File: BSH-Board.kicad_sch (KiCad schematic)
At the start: 10 parts, among them J1 667101210103, U1 ESP32-S2-MINI-2-N4, U3 TXS0102DQER, U5 AP63203WU

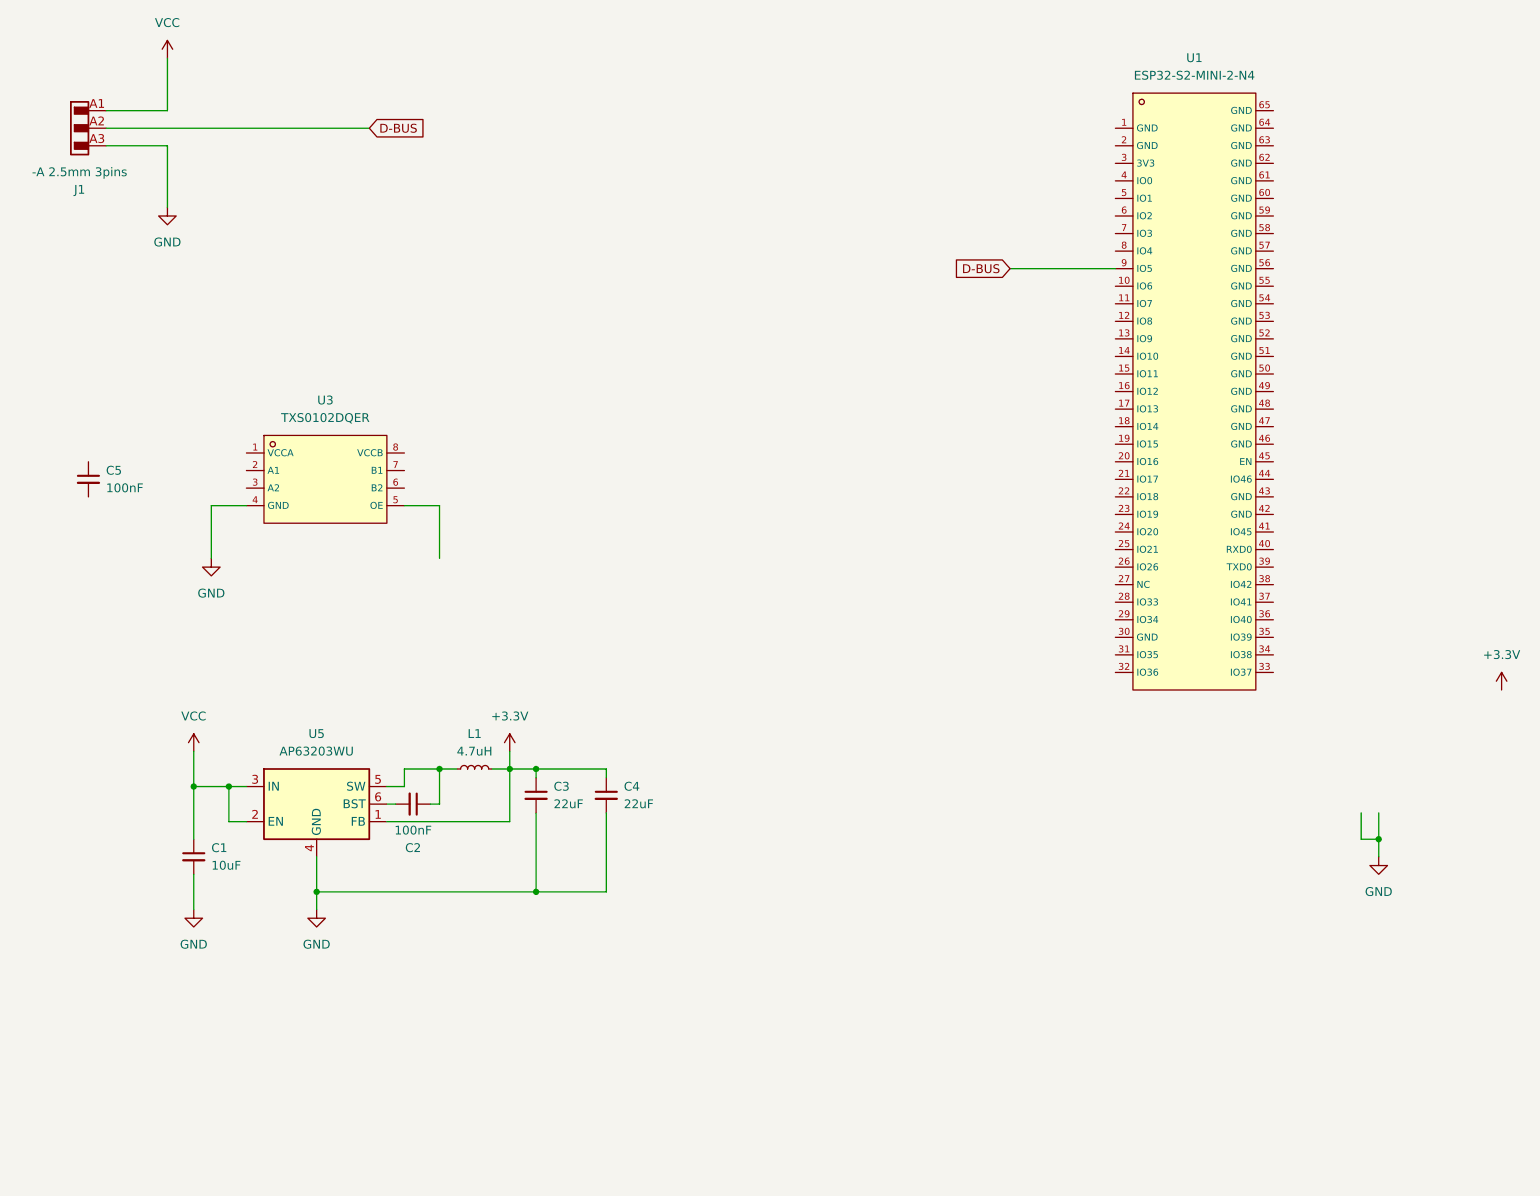
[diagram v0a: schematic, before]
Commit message: Add LDO for 5V
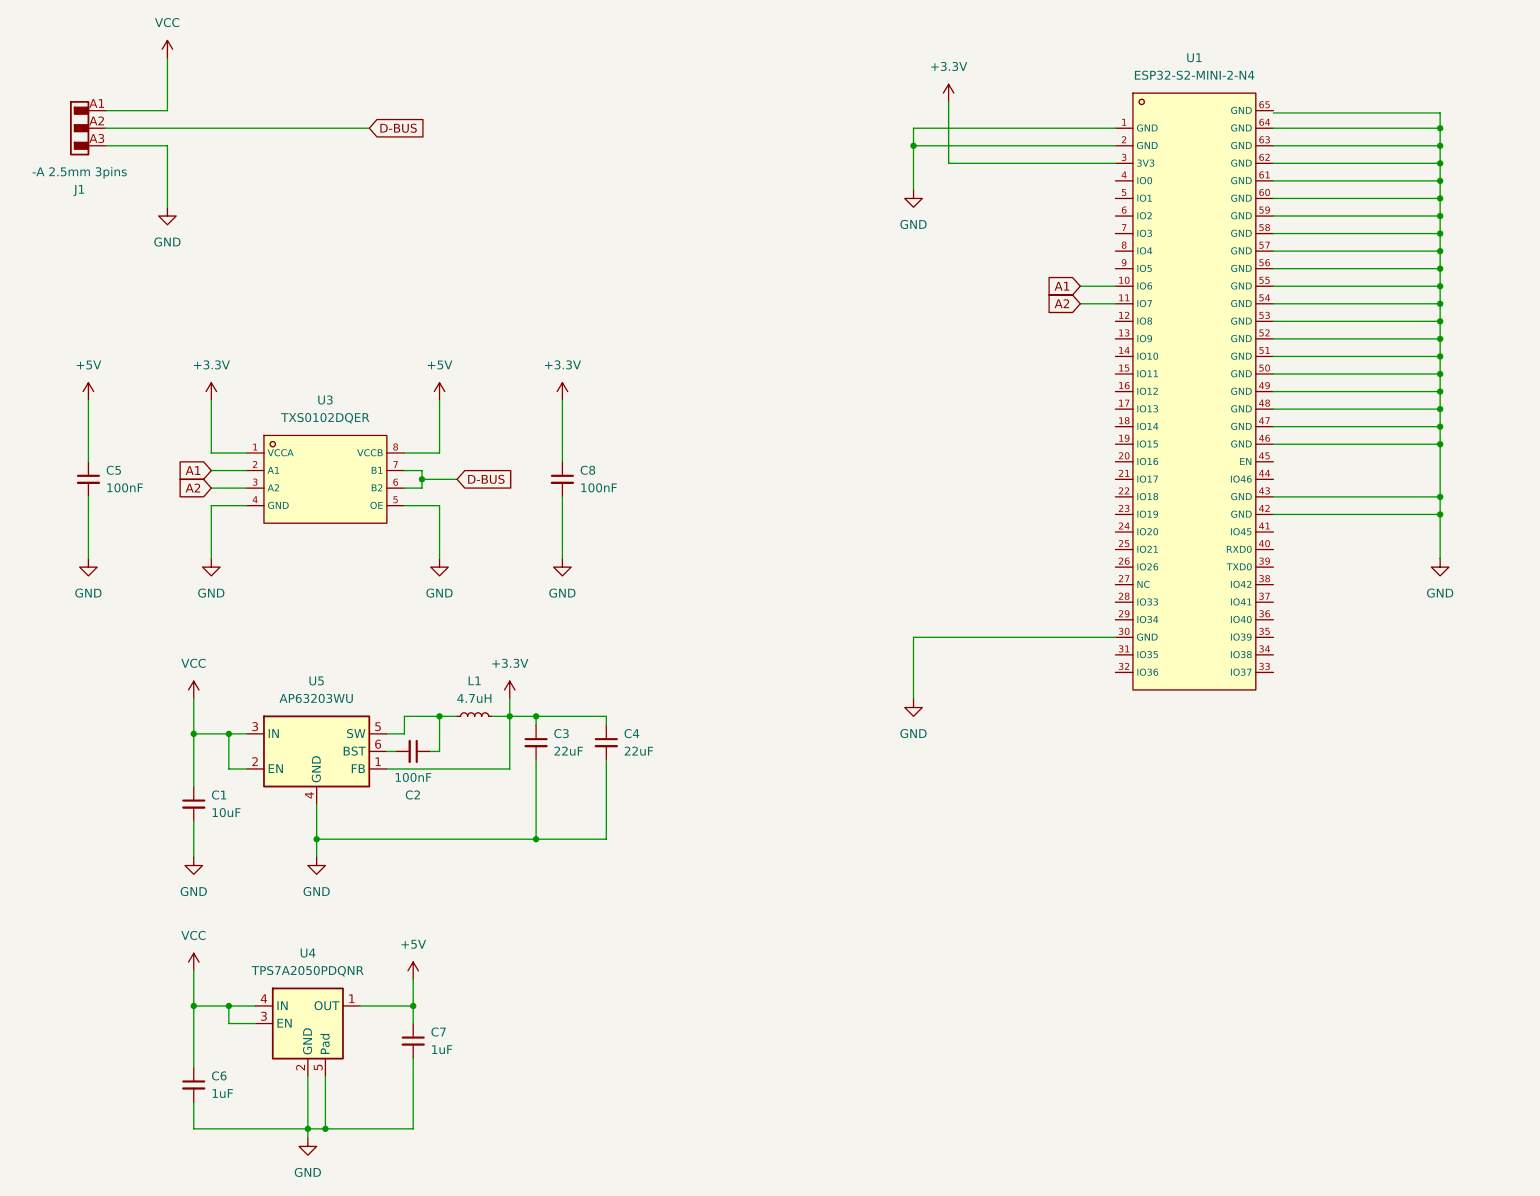
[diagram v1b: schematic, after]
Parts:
- added C6, C7: 1uF, Capacitor_SMD:C_0402_1005Metric, symbol Device:C_Small
- added C8: 100nF, Capacitor_SMD:C_0402_1005Metric, symbol Device:C_Small
- added U4: TPS7A2050PDQNR, Package_SON:Texas_X2SON-4_1x1mm_P0.65mm, symbol Regulator_Linear:TPS7A20xxxDQN
- C5: footprint Capacitor_SMD:C_0805_2012Metric -> Capacitor_SMD:C_0402_1005Metric; LCSC C45783 -> C1525
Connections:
- net +3.3V: now also U1.3 (3V3), U3.1 (VCCA), C8.1
- net D-BUS: now also U3.6 (B2), U3.7 (B1); no longer U1.9 (IO5)
- net GND: now also C5.2, U1.1 (GND), U1.2 (GND), U1.30 (GND), U1.42 (GND), U1.43 (GND), U1.46 (GND), U1.47 (GND), U1.48 (GND), U1.49 (GND), U1.50 (GND), U1.51 (GND), U1.52 (GND), U1.53 (GND), U1.54 (GND), U1.55 (GND), U1.56 (GND), U1.57 (GND), U1.58 (GND), U1.59 (GND), U1.60 (GND), U1.61 (GND), U1.62 (GND), U1.63 (GND), U1.64 (GND), U3.5 (OE), C6.2, C7.2, C8.2, U4.2 (GND), U4.5 (Pad)
- net VCC: now also C6.1, U4.3 (EN), U4.4 (IN)
- net A1: now reaches U1.10 (IO6)
- net A1: now also U3.2 (A1)
- net A2: now reaches U1.11 (IO7)
- net A2: now also U3.3 (A2)
- net +5V: now reaches U3.8 (VCCB)
- net +5V: now also C5.1, C7.1, U4.1 (OUT)
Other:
- moved on the sheet: C1, C2, C3, C4, L1, U5

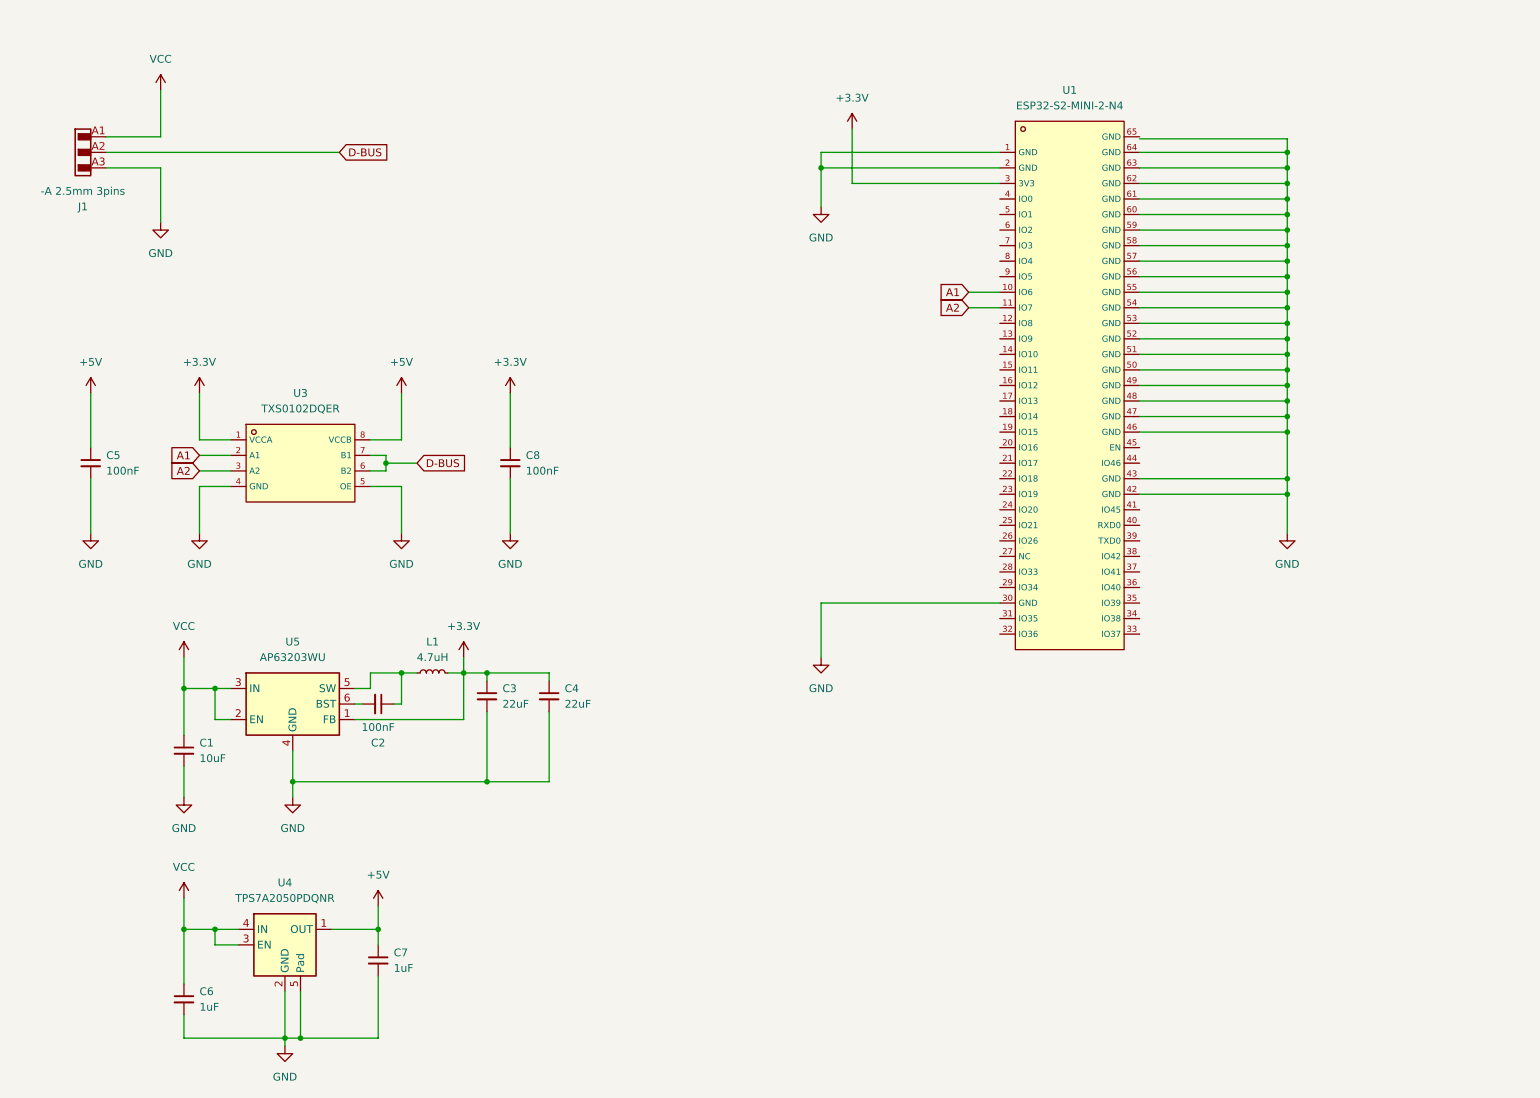
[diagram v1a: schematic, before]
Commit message: Added USB, replaced various parts
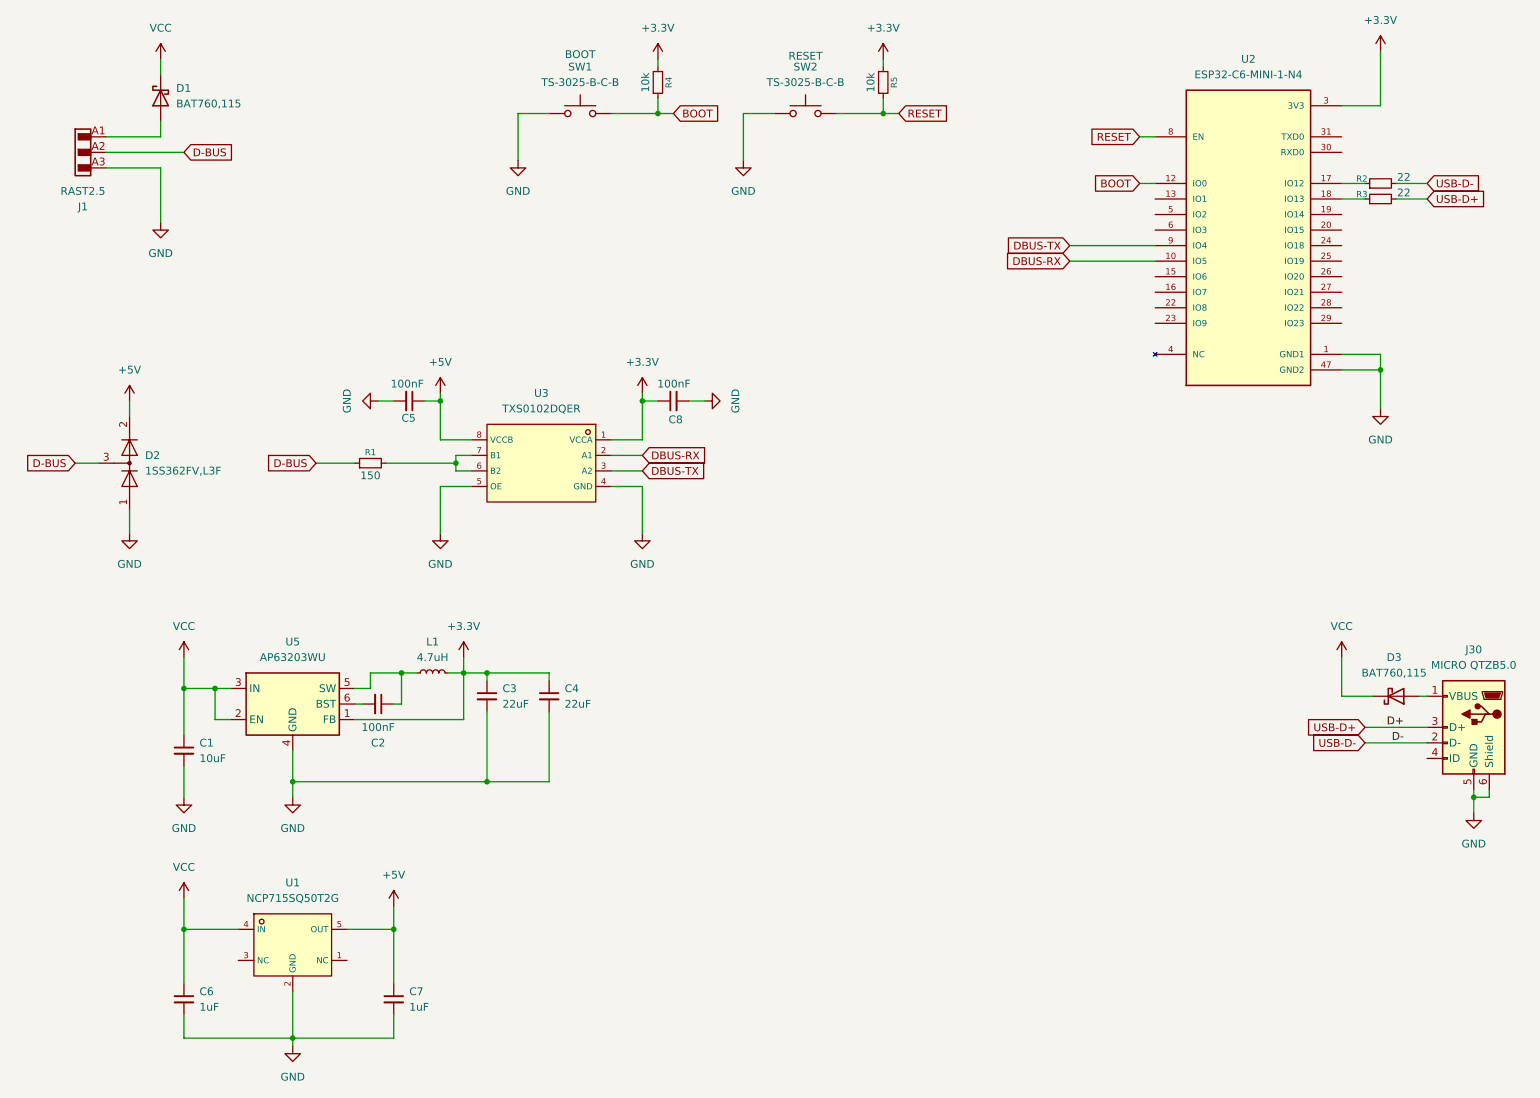
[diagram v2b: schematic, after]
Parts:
- removed U1: ESP32-S2-MINI-2-N4, footprints:WIFI-SMD_ESP32-MINI-1-N4, symbol ESP32-S2-MINI-2-N4:ESP32-S2-MINI-2-N4
- removed U4: TPS7A2050PDQNR, Package_SON:Texas_X2SON-4_1x1mm_P0.65mm, symbol Regulator_Linear:TPS7A20xxxDQN
- added D1, D3: BAT760,115, Diode_SMD:D_SOD-323, symbol Diode:1N5819WS
- added D2: 1SS362FV,L3F, Package_TO_SOT_SMD:SOT-723, symbol Diode:BAV99
- added J30: MICRO QTZB5.0, footprints:MICRO-USB-SMD_MICRO-QTZB5.0, symbol Connector:USB_B_Micro
- added R1: 150, Resistor_SMD:R_0402_1005Metric, symbol Device:R_Small
- added R2, R3: 22, Resistor_SMD:R_0402_1005Metric, symbol Device:R_Small
- added R4, R5: 10k, Resistor_SMD:R_0402_1005Metric, symbol Device:R_Small
- added SW1, SW2: TS-3025-B-C-B, footprints:SW-SMD_L3.0-W2.5-P3.40-LS4.0-L, symbol Switch:SW_Push
- added U1: NCP715SQ50T2G, Package_TO_SOT_SMD:SOT-353_SC-70-5, symbol NCP715SQ50T2G:NCP715SQ50T2G
- added U2: ESP32-C6-MINI-1-N4, footprints:XCVR_ESP32-C6-MINI-1-N4, symbol ESP32-C6-MINI-1-N4:ESP32-C6-MINI-1-N4
- J1: Critical Parameter -A 2.5mm 3pins -> RAST2.5
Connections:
- net +3.3V: now also R4.2, R5.2, U2.3 (3V3)
- net +5V: now also D2.2 (A), U1.5 (OUT)
- net D-BUS: now also D2.3 (K), R1.1; no longer U3.6 (B2), U3.7 (B1)
- net GND: now also D2.1 (K), J30.5 (GND), J30.6 (Shield), SW1.2, SW2.2, U1.2 (GND), U2.1 (GND1), U2.11 (GND1), U2.14 (GND1), U2.2 (GND1), U2.36 (GND1), U2.37 (GND1), U2.38 (GND1), U2.39 (GND1), U2.40 (GND1), U2.41 (GND1), U2.42 (GND1), U2.43 (GND1), U2.44 (GND1), U2.45 (GND1), U2.46 (GND1), U2.47 (GND2), U2.48 (GND2), U2.49_1 (GND2), U2.49_2 (GND2), U2.49_3 (GND2), U2.49_4 (GND2), U2.49_5 (GND2), U2.49_6 (GND2), U2.49_7 (GND2), U2.49_8 (GND2), U2.49_9 (GND2), U2.50 (GND2), U2.51 (GND2), U2.52 (GND2), U2.53 (GND2)
- net VCC: now also D1.1 (K), D3.1 (K), U1.4 (IN); no longer J1.A1, J1.B1
- net A1 renamed DBUS-RX
- net DBUS-RX: now also U2.10 (IO5)
- net A2 renamed DBUS-TX
- net DBUS-TX: now also U2.9 (IO4)
- new net: D1.2 (A), J1.A1, J1.B1
- new net: D3.2 (A), J30.1 (VBUS)
- new net: R2.1, U2.17 (IO12)
- new net: R3.1, U2.18 (IO13)
- new net: U2.21 (NC), U2.32 (NC), U2.33 (NC), U2.34 (NC), U2.35 (NC), U2.4 (NC), U2.7 (NC)
- new net: R1.2, U3.6 (B2), U3.7 (B1)
- new net BOOT: R4.1, SW1.1, U2.12 (IO0)
- new net RESET: R5.1, SW2.1, U2.8 (EN)
- new net USB-D+: J30.3 (D+), R3.2
- new net USB-D-: J30.2 (D-), R2.2
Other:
- moved on the sheet: C5, C7, C8, U3
